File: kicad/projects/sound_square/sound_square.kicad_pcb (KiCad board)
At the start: 2 copper layers, 203.2 x 97.8 mm, 9 parts, among them J1 peripheral_addr_bus_connector, J2 peripheral_aux_connector, J3 peripheral_membank_connector

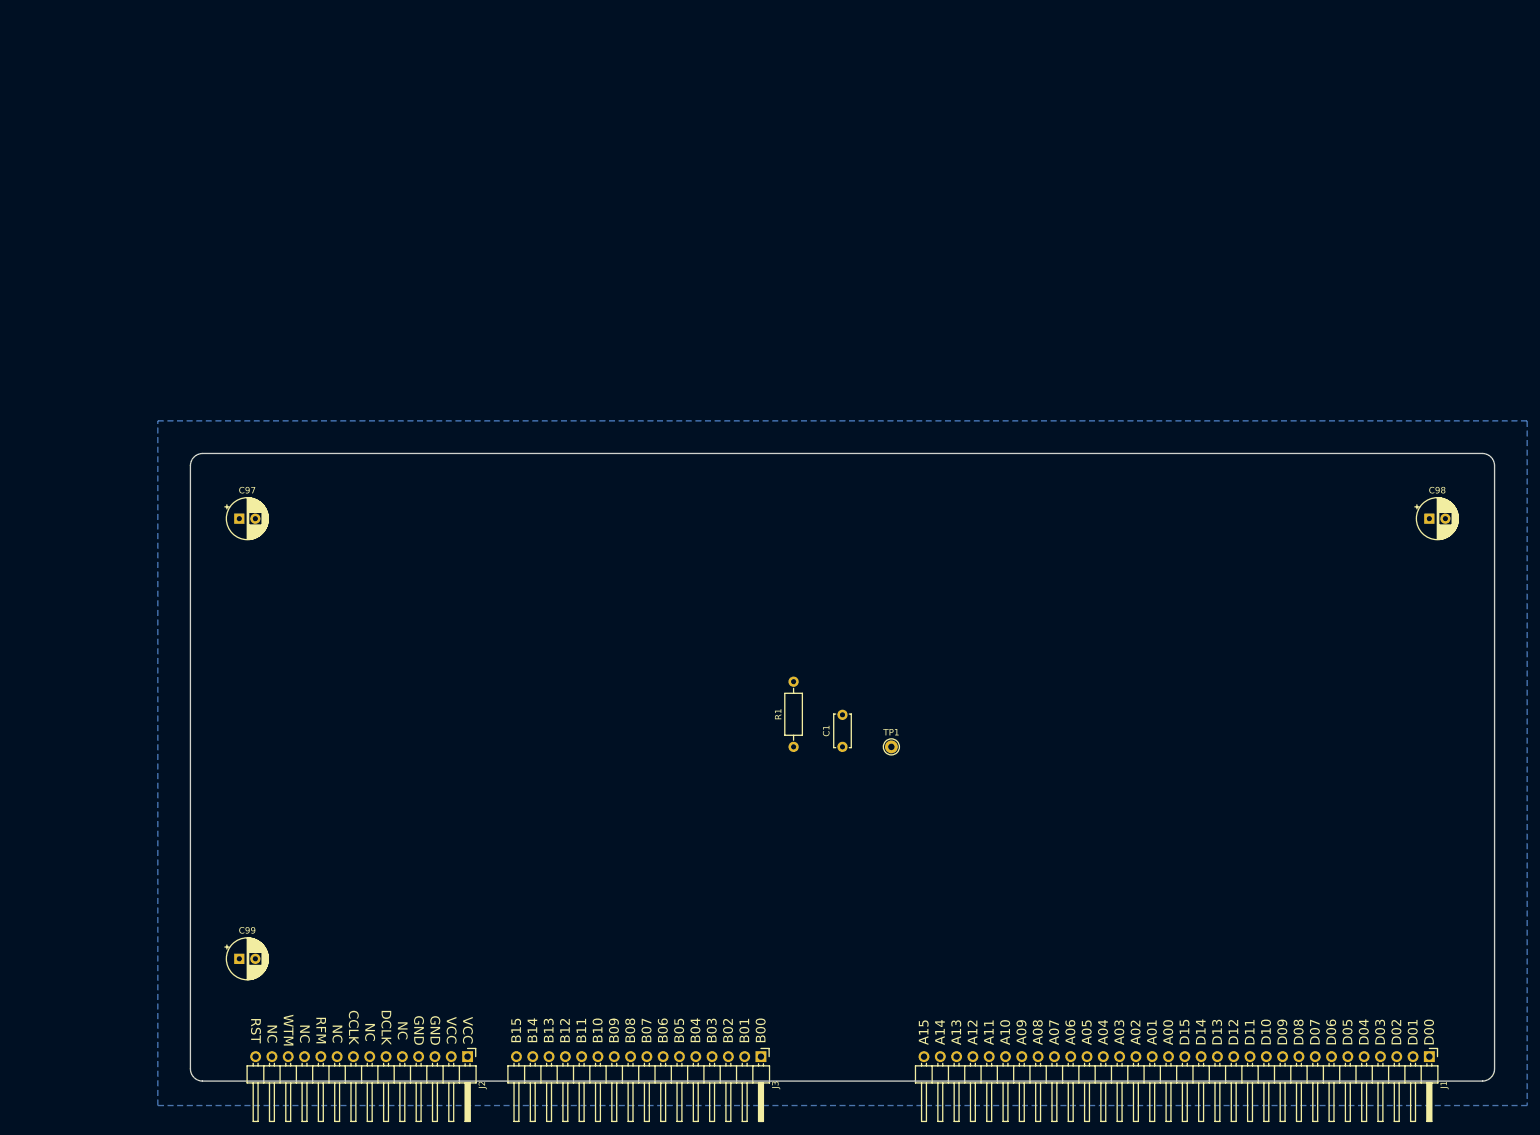
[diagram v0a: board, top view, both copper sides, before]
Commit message: Progress on sound square schematic and PCB.
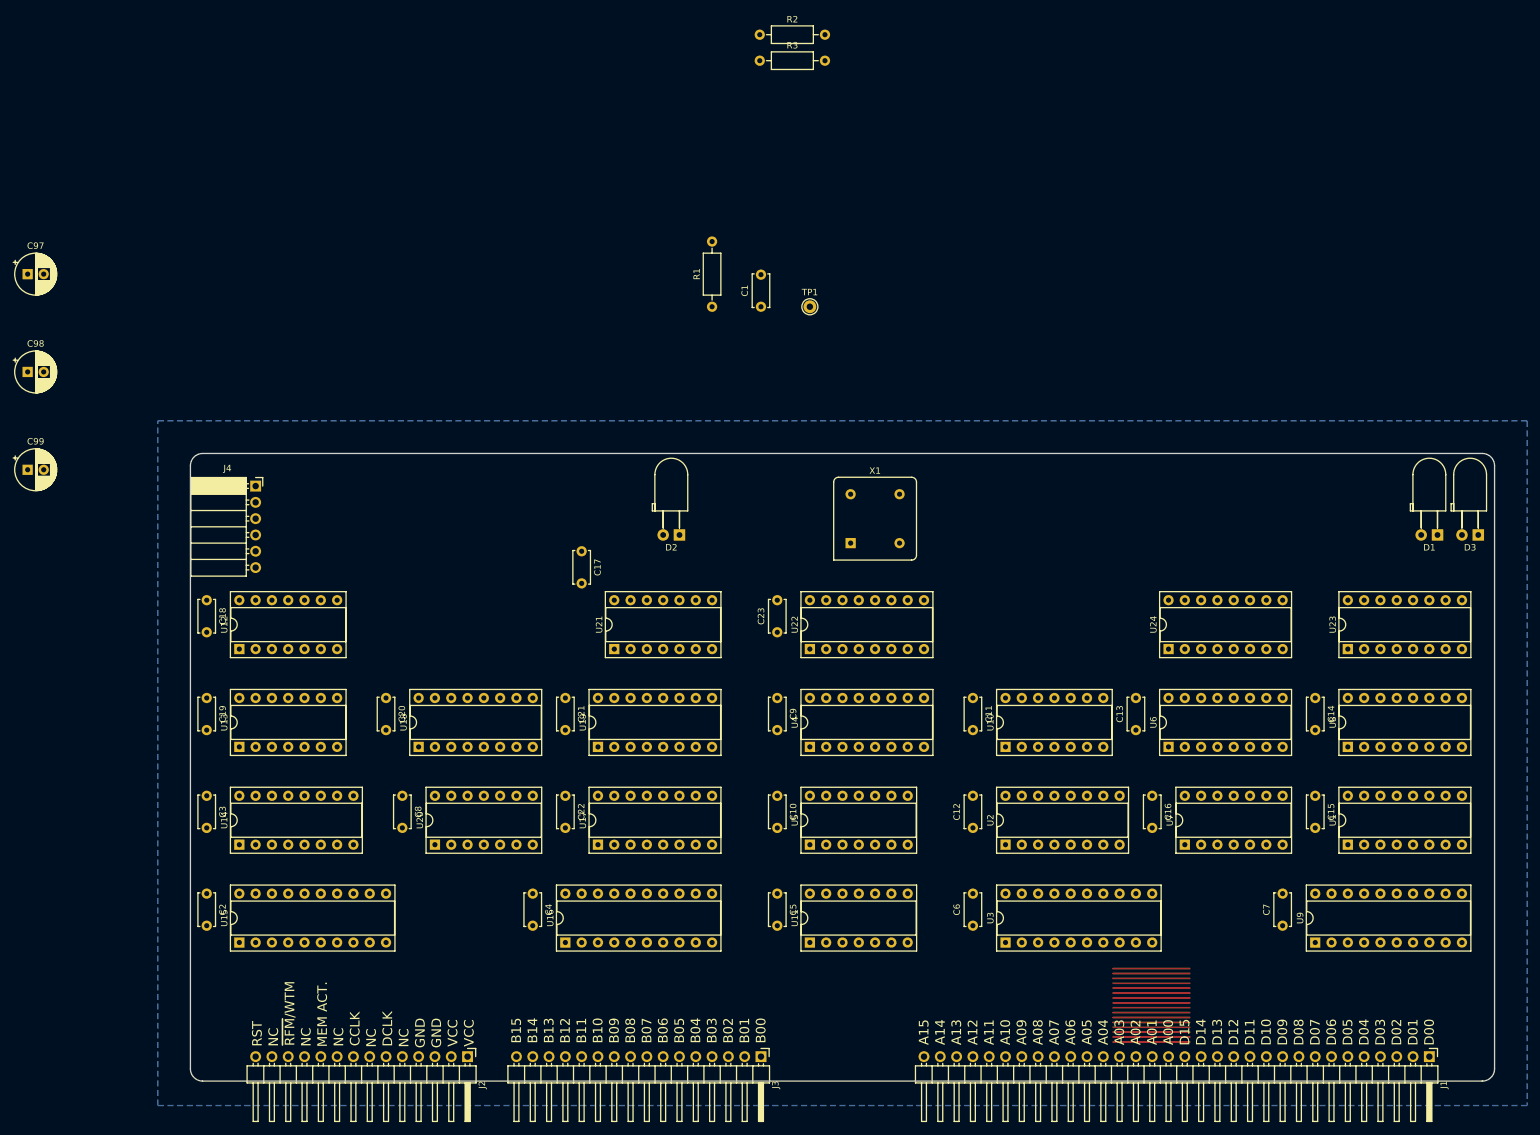
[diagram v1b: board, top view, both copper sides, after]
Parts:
- added C10: C, Capacitor_THT:C_Disc_D5.0mm_W2.5mm_P5.00mm, F.Cu at (142.2, 104.1)
- added C11: C, Capacitor_THT:C_Disc_D5.0mm_W2.5mm_P5.00mm, F.Cu at (172.7, 88.9)
- added C12: C, Capacitor_THT:C_Disc_D5.0mm_W2.5mm_P5.00mm, F.Cu at (172.7, 109.1)
- added C13: C, Capacitor_THT:C_Disc_D5.0mm_W2.5mm_P5.00mm, F.Cu at (198.1, 93.9)
- added C14: C, Capacitor_THT:C_Disc_D5.0mm_W2.5mm_P5.00mm, F.Cu at (226.1, 88.9)
- added C15: C, Capacitor_THT:C_Disc_D5.0mm_W2.5mm_P5.00mm, F.Cu at (226.1, 104.1)
- added C16: C, Capacitor_THT:C_Disc_D5.0mm_W2.5mm_P5.00mm, F.Cu at (200.7, 104.1)
- added C17: C, Capacitor_THT:C_Disc_D5.0mm_W2.5mm_P5.00mm, F.Cu at (111.8, 66.0)
- added C18: C, Capacitor_THT:C_Disc_D5.0mm_W2.5mm_P5.00mm, F.Cu at (53.3, 73.7)
- added C19: C, Capacitor_THT:C_Disc_D5.0mm_W2.5mm_P5.00mm, F.Cu at (53.3, 88.9)
- added C2: C, Capacitor_THT:C_Disc_D5.0mm_W2.5mm_P5.00mm, F.Cu at (53.3, 119.4)
- added C20: C, Capacitor_THT:C_Disc_D5.0mm_W2.5mm_P5.00mm, F.Cu at (81.3, 88.9)
- added C21: C, Capacitor_THT:C_Disc_D5.0mm_W2.5mm_P5.00mm, F.Cu at (109.2, 88.9)
- added C22: C, Capacitor_THT:C_Disc_D5.0mm_W2.5mm_P5.00mm, F.Cu at (109.2, 104.1)
- added C23: C, Capacitor_THT:C_Disc_D5.0mm_W2.5mm_P5.00mm, F.Cu at (142.2, 78.7)
- added C3: C, Capacitor_THT:C_Disc_D5.0mm_W2.5mm_P5.00mm, F.Cu at (53.3, 104.1)
- added C4: C, Capacitor_THT:C_Disc_D5.0mm_W2.5mm_P5.00mm, F.Cu at (104.1, 119.4)
- added C5: C, Capacitor_THT:C_Disc_D5.0mm_W2.5mm_P5.00mm, F.Cu at (142.2, 119.4)
- added C6: C, Capacitor_THT:C_Disc_D5.0mm_W2.5mm_P5.00mm, F.Cu at (172.7, 124.4)
- added C7: C, Capacitor_THT:C_Disc_D5.0mm_W2.5mm_P5.00mm, F.Cu at (221.0, 124.4)
- added C8: C, Capacitor_THT:C_Disc_D5.0mm_W2.5mm_P5.00mm, F.Cu at (83.8, 104.1)
- added C9: C, Capacitor_THT:C_Disc_D5.0mm_W2.5mm_P5.00mm, F.Cu at (142.2, 88.9)
- added D1: LED, sixteen-bit-computer:LED_D5.0mm_Horizontal_O3.81mm_Z3.0mm, F.Cu at (245.1, 63.5)
- added D2: LED, sixteen-bit-computer:LED_D5.0mm_Horizontal_O3.81mm_Z3.0mm, F.Cu at (127.0, 63.5)
- added D3: LED, sixteen-bit-computer:LED_D5.0mm_Horizontal_O3.81mm_Z3.0mm, F.Cu at (251.5, 63.5)
- added J4: Conn_01x06_Socket, Connector_PinSocket_2.54mm:PinSocket_1x06_P2.54mm_Horizontal, F.Cu at (61.0, 55.9)
- added R2: R_US, Resistor_THT:R_Axial_DIN0207_L6.3mm_D2.5mm_P10.16mm_Horizontal, F.Cu at (139.5, -14.4)
- added R3: 10K, Resistor_THT:R_Axial_DIN0207_L6.3mm_D2.5mm_P10.16mm_Horizontal, F.Cu at (139.5, -10.4)
- added U1: 74HC40103, Package_DIP:DIP-16_W7.62mm_Socket, F.Cu at (231.1, 111.8)
- added U10: 74HC08, Package_DIP:DIP-14_W7.62mm_Socket, F.Cu at (177.8, 96.5)
- added U11: 74HC32, Package_DIP:DIP-14_W7.62mm_Socket, F.Cu at (147.3, 127.0)
- added U12: 74HC02, Package_DIP:DIP-14_W7.62mm_Socket, F.Cu at (58.4, 81.3)
- added U13: 74HC08, Package_DIP:DIP-14_W7.62mm_Socket, F.Cu at (58.4, 96.5)
- added U14: 74HC40103, Package_DIP:DIP-16_W7.62mm_Socket, F.Cu at (58.4, 111.8)
- added U15: 74HC273, Package_DIP:DIP-20_W7.62mm_Socket, F.Cu at (58.4, 127.0)
- added U16: 74HC574, Package_DIP:DIP-20_W7.62mm_Socket, F.Cu at (109.2, 127.0)
- added U17: 74HC40103, Package_DIP:DIP-16_W7.62mm_Socket, F.Cu at (114.3, 111.8)
- added U18: 74HC157, Package_DIP:DIP-16_W7.62mm_Socket, F.Cu at (86.4, 96.5)
- added U19: 74HC157, Package_DIP:DIP-16_W7.62mm_Socket, F.Cu at (114.3, 96.5)
- added U2: 74HC40103, Package_DIP:DIP-16_W7.62mm_Socket, F.Cu at (177.8, 111.8)
- added U20: 74HC04, Package_DIP:DIP-14_W7.62mm_Socket, F.Cu at (88.9, 111.8)
- added U21: 74HC11, Package_DIP:DIP-14_W7.62mm_Socket, F.Cu at (116.8, 81.3)
- added U22: 74HC161, Package_DIP:DIP-16_W7.62mm_Socket, F.Cu at (147.3, 81.3)
- added U23: 74HC238, Package_DIP:DIP-16_W7.62mm_Socket, F.Cu at (231.1, 81.3)
- added U24: 74HC238, Package_DIP:DIP-16_W7.62mm_Socket, F.Cu at (203.2, 81.3)
- added U3: 74HC273, Package_DIP:DIP-20_W7.62mm_Socket, F.Cu at (177.8, 127.0)
- added U4: 74HC109, Package_DIP:DIP-16_W7.62mm_Socket, F.Cu at (147.3, 96.5)
- added U5: 74HC02, Package_DIP:DIP-14_W7.62mm_Socket, F.Cu at (147.3, 111.8)
- added U6: 74HC157, Package_DIP:DIP-16_W7.62mm_Socket, F.Cu at (203.2, 96.5)
- added U7: 74HC04, Package_DIP:DIP-14_W7.62mm_Socket, F.Cu at (205.7, 111.8)
- added U8: 74HC157, Package_DIP:DIP-16_W7.62mm_Socket, F.Cu at (231.1, 96.5)
- added U9: 74HC574, Package_DIP:DIP-20_W7.62mm_Socket, F.Cu at (226.1, 127.0)
- added X1: CXO_DIP8, Oscillator:Oscillator_DIP-8, F.Cu at (153.7, 64.8)
- R1: value R_US -> 10K
- moved C98 219.6 mm to (25.4, 38.1)
- moved C99 83.0 mm to (25.4, 53.3)
- moved C1 69.7 mm to (139.7, 27.9)
- moved R1 69.7 mm to (132.1, 27.9)
- moved TP1 69.7 mm to (147.3, 27.9)
- moved C97 50.4 mm to (25.4, 22.9)
- turned J2 to 0 degrees
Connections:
- J1 pad 17: /ADDR_BUS_00 -> unconnected-(J1-A_00-Pad17)
- J1 pad 18: /ADDR_BUS_01 -> unconnected-(J1-A_01-Pad18)
- J1 pad 19: /ADDR_BUS_02 -> unconnected-(J1-A_02-Pad19)
- J1 pad 20: /ADDR_BUS_03 -> unconnected-(J1-A_03-Pad20)
- J1 pad 21: /ADDR_BUS_04 -> unconnected-(J1-A_04-Pad21)
- J1 pad 22: /ADDR_BUS_05 -> unconnected-(J1-A_05-Pad22)
- J1 pad 23: /ADDR_BUS_06 -> unconnected-(J1-A_06-Pad23)
- J1 pad 24: /ADDR_BUS_07 -> unconnected-(J1-A_07-Pad24)
- J1 pad 25: /ADDR_BUS_08 -> unconnected-(J1-A_08-Pad25)
- J1 pad 26: /ADDR_BUS_09 -> unconnected-(J1-A_09-Pad26)
- J1 pad 27: /ADDR_BUS_10 -> unconnected-(J1-A_10-Pad27)
- J1 pad 28: /ADDR_BUS_11 -> unconnected-(J1-A_11-Pad28)
- J1 pad 29: /ADDR_BUS_12 -> unconnected-(J1-A_12-Pad29)
- J1 pad 30: /ADDR_BUS_13 -> unconnected-(J1-A_13-Pad30)
- J1 pad 31: /ADDR_BUS_14 -> unconnected-(J1-A_14-Pad31)
- J1 pad 32: /ADDR_BUS_15 -> unconnected-(J1-A_15-Pad32)
- J2 pad 10: /RFM -> /MEM_ACT
- J2 pad 12: /WTM -> /~{RFM}/WTM
- J2 pad 8: /CTL_CLK -> unconnected-(J2-CCLK-Pad8)
- J3 pad 1: /BANK_BUS_00 -> unconnected-(J3-B_00-Pad1)
- J3 pad 10: /BANK_BUS_09 -> unconnected-(J3-B_09-Pad10)
- J3 pad 11: /BANK_BUS_10 -> unconnected-(J3-B_10-Pad11)
- J3 pad 12: /BANK_BUS_11 -> unconnected-(J3-B_11-Pad12)
- J3 pad 13: /BANK_BUS_12 -> unconnected-(J3-B_12-Pad13)
- J3 pad 14: /BANK_BUS_13 -> unconnected-(J3-B_13-Pad14)
- J3 pad 15: /BANK_BUS_14 -> unconnected-(J3-B_14-Pad15)
- J3 pad 16: /BANK_BUS_15 -> unconnected-(J3-B_15-Pad16)
- J3 pad 2: /BANK_BUS_01 -> unconnected-(J3-B_01-Pad2)
- J3 pad 3: /BANK_BUS_02 -> unconnected-(J3-B_02-Pad3)
- J3 pad 4: /BANK_BUS_03 -> unconnected-(J3-B_03-Pad4)
- J3 pad 5: /BANK_BUS_04 -> unconnected-(J3-B_04-Pad5)
- J3 pad 6: /BANK_BUS_05 -> unconnected-(J3-B_05-Pad6)
- J3 pad 7: /BANK_BUS_06 -> unconnected-(J3-B_06-Pad7)
- J3 pad 8: /BANK_BUS_07 -> unconnected-(J3-B_07-Pad8)
- J3 pad 9: /BANK_BUS_08 -> unconnected-(J3-B_08-Pad9)
- R1 pad 1: unconnected-(R1-Pad1) -> GND
- R1 pad 2: unconnected-(R1-Pad2) -> /CHANNEL_A_ADDRESSED
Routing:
- net (no net): track 0.00 -> 191.0 mm

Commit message: Add led output and clock divider to sound square.
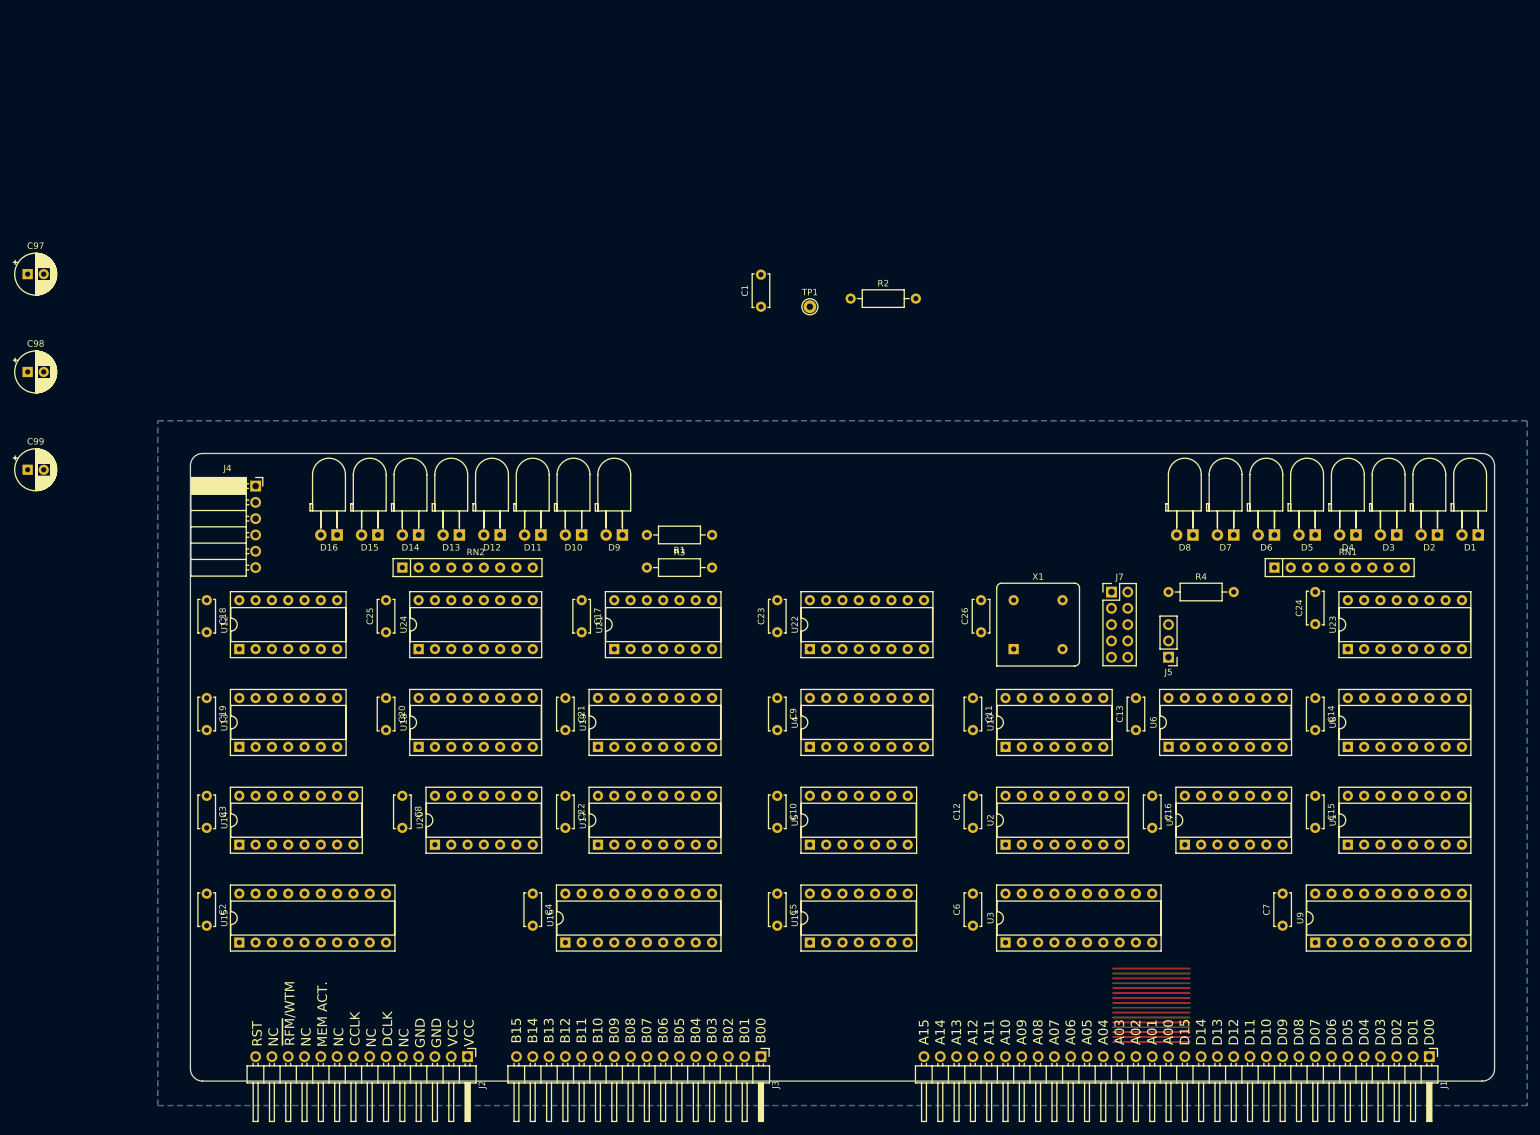
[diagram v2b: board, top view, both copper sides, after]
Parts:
- added C24: C, Capacitor_THT:C_Disc_D5.0mm_W2.5mm_P5.00mm, F.Cu at (226.1, 77.4)
- added C25: C, Capacitor_THT:C_Disc_D5.0mm_W2.5mm_P5.00mm, F.Cu at (81.3, 78.7)
- added C26: C, Capacitor_THT:C_Disc_D5.0mm_W2.5mm_P5.00mm, F.Cu at (174.0, 78.7)
- added D10: LED, sixteen-bit-computer:LED_D5.0mm_Horizontal_O3.81mm_Z3.0mm, F.Cu at (111.8, 63.5)
- added D11: LED, sixteen-bit-computer:LED_D5.0mm_Horizontal_O3.81mm_Z3.0mm, F.Cu at (105.4, 63.5)
- added D12: LED, sixteen-bit-computer:LED_D5.0mm_Horizontal_O3.81mm_Z3.0mm, F.Cu at (99.1, 63.5)
- added D13: LED, sixteen-bit-computer:LED_D5.0mm_Horizontal_O3.81mm_Z3.0mm, F.Cu at (92.7, 63.5)
- added D14: LED, sixteen-bit-computer:LED_D5.0mm_Horizontal_O3.81mm_Z3.0mm, F.Cu at (86.4, 63.5)
- added D15: LED, sixteen-bit-computer:LED_D5.0mm_Horizontal_O3.81mm_Z3.0mm, F.Cu at (80.0, 63.5)
- added D16: LED, sixteen-bit-computer:LED_D5.0mm_Horizontal_O3.81mm_Z3.0mm, F.Cu at (73.7, 63.5)
- added D4: LED, sixteen-bit-computer:LED_D5.0mm_Horizontal_O3.81mm_Z3.0mm, F.Cu at (232.4, 63.5)
- added D5: LED, sixteen-bit-computer:LED_D5.0mm_Horizontal_O3.81mm_Z3.0mm, F.Cu at (226.1, 63.5)
- added D6: LED, sixteen-bit-computer:LED_D5.0mm_Horizontal_O3.81mm_Z3.0mm, F.Cu at (219.7, 63.5)
- added D7: LED, sixteen-bit-computer:LED_D5.0mm_Horizontal_O3.81mm_Z3.0mm, F.Cu at (213.4, 63.5)
- added D8: LED, sixteen-bit-computer:LED_D5.0mm_Horizontal_O3.81mm_Z3.0mm, F.Cu at (207.0, 63.5)
- added D9: LED, sixteen-bit-computer:LED_D5.0mm_Horizontal_O3.81mm_Z3.0mm, F.Cu at (118.1, 63.5)
- added J5: Conn_01x03_Pin, Connector_PinHeader_2.54mm:PinHeader_1x03_P2.54mm_Vertical, F.Cu at (203.2, 82.5)
- added J7: Conn_02x05_Odd_Even, Connector_PinHeader_2.54mm:PinHeader_2x05_P2.54mm_Vertical, F.Cu at (194.3, 72.4)
- added R4: 10K, Resistor_THT:R_Axial_DIN0207_L6.3mm_D2.5mm_P10.16mm_Horizontal, F.Cu at (203.2, 72.4)
- added RN1: R_Network08_US, Resistor_THT:R_Array_SIP9, F.Cu at (219.7, 68.6)
- added RN2: R_Network08_US, Resistor_THT:R_Array_SIP9, F.Cu at (83.8, 68.6)
- moved D2 118.1 mm to (245.1, 63.5)
- moved U24 116.8 mm to (86.4, 81.3)
- moved R3 80.9 mm to (121.9, 68.6)
- moved R2 43.5 mm to (153.7, 26.7)
- moved R1 35.6 mm to (132.1, 63.5), turned to 180 degrees
- moved X1 30.3 mm to (179.1, 81.3)
- moved D3 12.7 mm to (238.8, 63.5)
- moved C17 7.62 mm to (111.8, 73.7)
- moved D1 6.35 mm to (251.5, 63.5)
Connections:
- C23 pad 1: unconnected-(C23-Pad1) -> GND
- C23 pad 2: Net-(U22-VCC) -> VCC
- D1 pad 1: unconnected-(D1-K-Pad1) -> Net-(D1-K)
- D1 pad 2: unconnected-(D1-A-Pad2) -> Net-(D1-A)
- D2 pad 1: unconnected-(D2-K-Pad1) -> Net-(D2-K)
- D2 pad 2: unconnected-(D2-A-Pad2) -> Net-(D2-A)
- D3 pad 1: unconnected-(D3-K-Pad1) -> Net-(D3-K)
- D3 pad 2: unconnected-(D3-A-Pad2) -> Net-(D3-A)
- U1 pad 1: Net-(U1-CP) -> /CHOSEN_CLK
- U1 pad 3: unconnected-(U1-~{TE}-Pad3) -> GND
- U14 pad 1: Net-(U14-CP) -> /CHOSEN_CLK
- U17 pad 1: Net-(U14-CP) -> /CHOSEN_CLK
- U17 pad 3: unconnected-(U17-~{TE}-Pad3) -> GND
- U2 pad 1: Net-(U1-CP) -> /CHOSEN_CLK
- U22 pad 1: unconnected-(U22-~{MR}-Pad1) -> VCC
- U22 pad 10: unconnected-(U22-TE-Pad10) -> VCC
- U22 pad 11: unconnected-(U22-Q3-Pad11) -> /CLOCK_BY_16
- U22 pad 12: unconnected-(U22-Q2-Pad12) -> /CLOCK_BY_8
- U22 pad 13: unconnected-(U22-Q1-Pad13) -> /CLOCK_BY_4
- U22 pad 14: unconnected-(U22-Q0-Pad14) -> /CLOCK_BY_2
- U22 pad 16: Net-(U22-VCC) -> VCC
- U22 pad 2: unconnected-(U22-CP-Pad2) -> /CRYSTAL_CLOCK
- U22 pad 3: unconnected-(U22-P0-Pad3) -> GND
- U22 pad 4: unconnected-(U22-P1-Pad4) -> GND
- U22 pad 5: unconnected-(U22-P2-Pad5) -> GND
- U22 pad 6: unconnected-(U22-P3-Pad6) -> GND
- U22 pad 7: unconnected-(U22-PE-Pad7) -> VCC
- U22 pad 8: unconnected-(U22-GND-Pad8) -> GND
- U22 pad 9: unconnected-(U22-~{SPE}-Pad9) -> VCC
- U23 pad 10: unconnected-(U23-Y5-Pad10) -> Net-(D6-A)
- U23 pad 11: unconnected-(U23-Y4-Pad11) -> Net-(D5-A)
- U23 pad 12: unconnected-(U23-Y3-Pad12) -> Net-(D4-A)
- U23 pad 13: unconnected-(U23-Y2-Pad13) -> Net-(D3-A)
- U23 pad 14: unconnected-(U23-Y1-Pad14) -> Net-(D2-A)
- U23 pad 15: unconnected-(U23-Y0-Pad15) -> Net-(D1-A)
- U23 pad 16: unconnected-(U23-VCC-Pad16) -> VCC
- U23 pad 4: unconnected-(U23-~{E1}-Pad4) -> GND
- U23 pad 5: unconnected-(U23-~{E2}-Pad5) -> GND
- U23 pad 6: unconnected-(U23-E3-Pad6) -> VCC
- U23 pad 7: unconnected-(U23-Y7-Pad7) -> Net-(D8-A)
- U23 pad 8: unconnected-(U23-GND-Pad8) -> GND
- U23 pad 9: unconnected-(U23-Y6-Pad9) -> Net-(D7-A)
- U24 pad 10: unconnected-(U24-Y5-Pad10) -> Net-(D14-A)
- U24 pad 11: unconnected-(U24-Y4-Pad11) -> Net-(D13-A)
- U24 pad 12: unconnected-(U24-Y3-Pad12) -> Net-(D12-A)
- U24 pad 13: unconnected-(U24-Y2-Pad13) -> Net-(D11-A)
- U24 pad 14: unconnected-(U24-Y1-Pad14) -> Net-(D10-A)
- U24 pad 15: unconnected-(U24-Y0-Pad15) -> Net-(D9-A)
- U24 pad 16: unconnected-(U24-VCC-Pad16) -> VCC
- U24 pad 4: unconnected-(U24-~{E1}-Pad4) -> GND
- U24 pad 5: unconnected-(U24-~{E2}-Pad5) -> GND
- U24 pad 6: unconnected-(U24-E3-Pad6) -> VCC
- U24 pad 7: unconnected-(U24-Y7-Pad7) -> Net-(D16-A)
- U24 pad 8: unconnected-(U24-GND-Pad8) -> GND
- U24 pad 9: unconnected-(U24-Y6-Pad9) -> Net-(D15-A)
- X1 pad 4: unconnected-(X1-GND-Pad4) -> GND
- X1 pad 5: unconnected-(X1-OUT-Pad5) -> /CRYSTAL_CLOCK
- X1 pad 8: unconnected-(X1-Vcc-Pad8) -> VCC
